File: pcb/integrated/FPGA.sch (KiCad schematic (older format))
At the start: 28 parts, among them J3001 Conn_01x04_Male, J3002 Conn_01x06_Male, U3001 XC7S25-L1FTGB196, U3002 S25FL127SABN, U3003 74AVC4TD245BQ

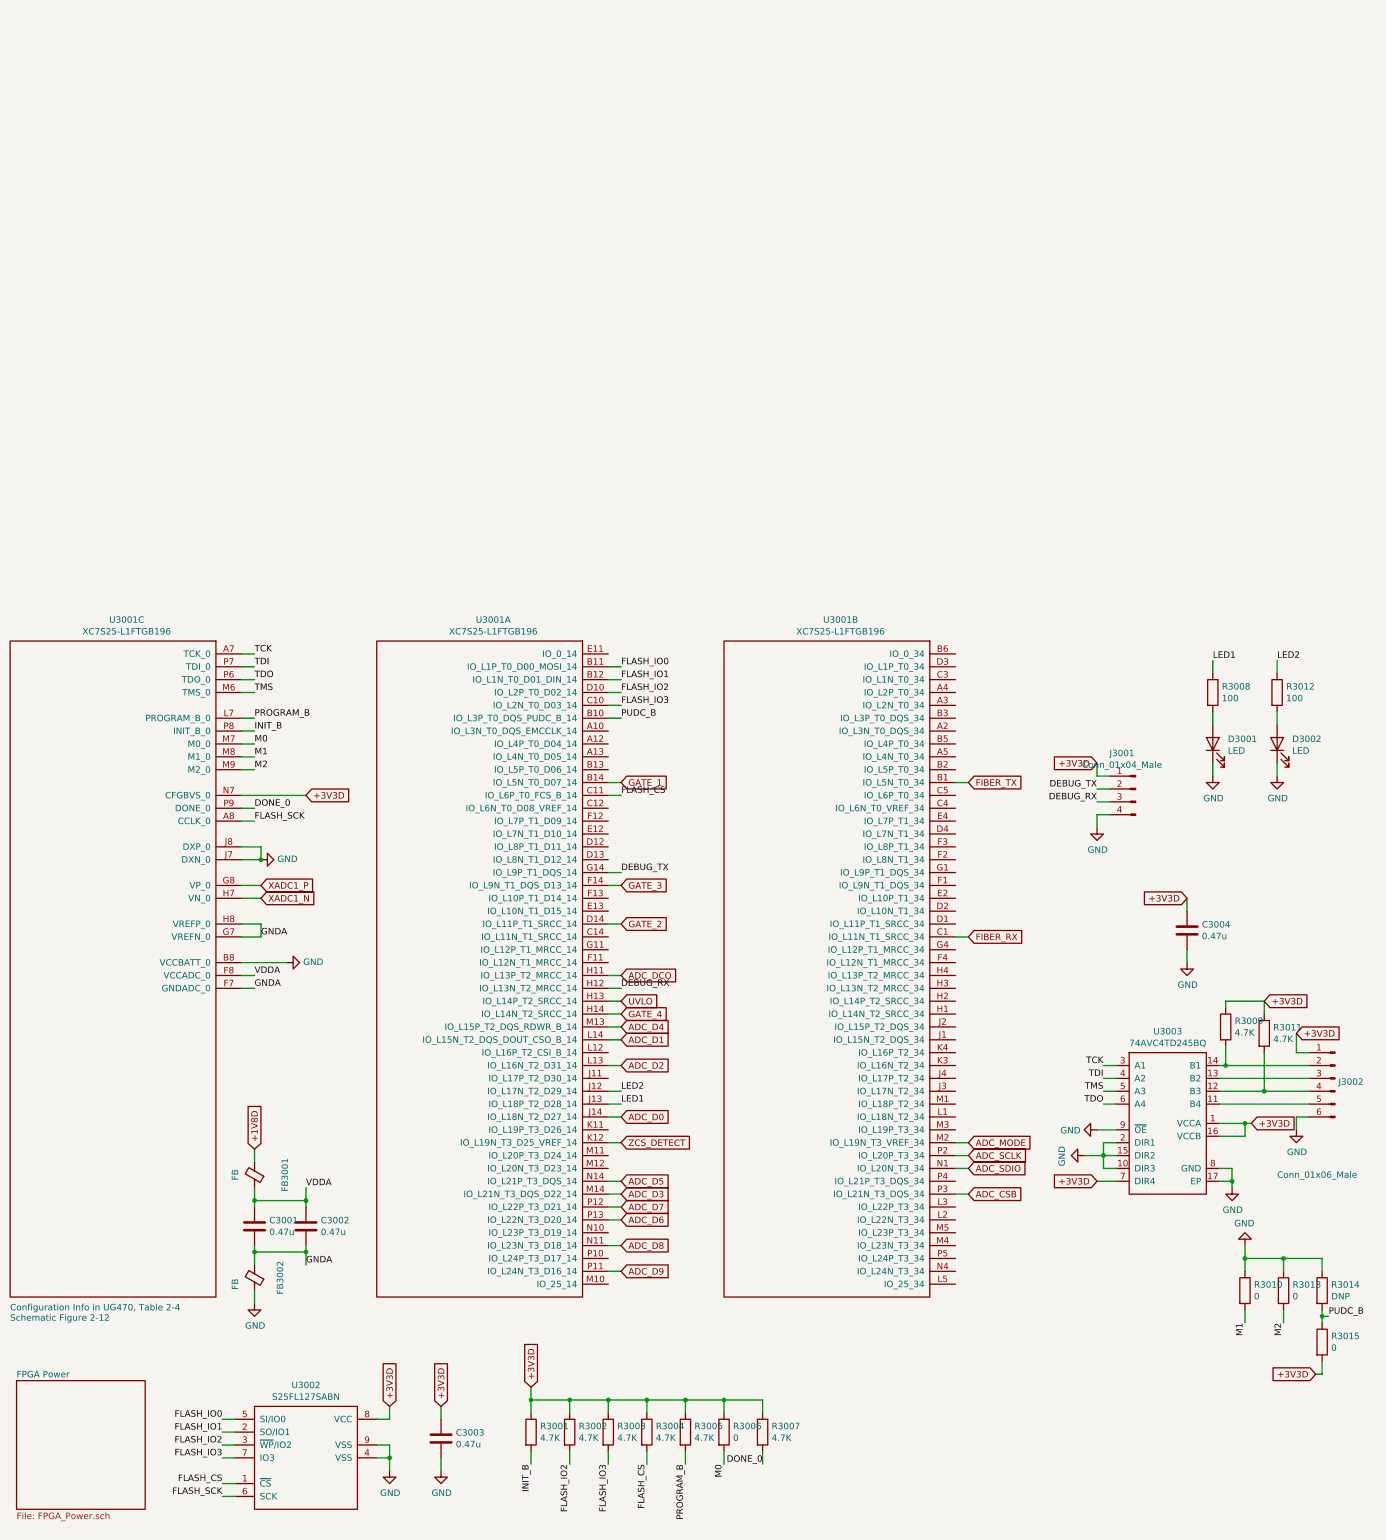
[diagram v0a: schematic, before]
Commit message: schematic fixes and component placement
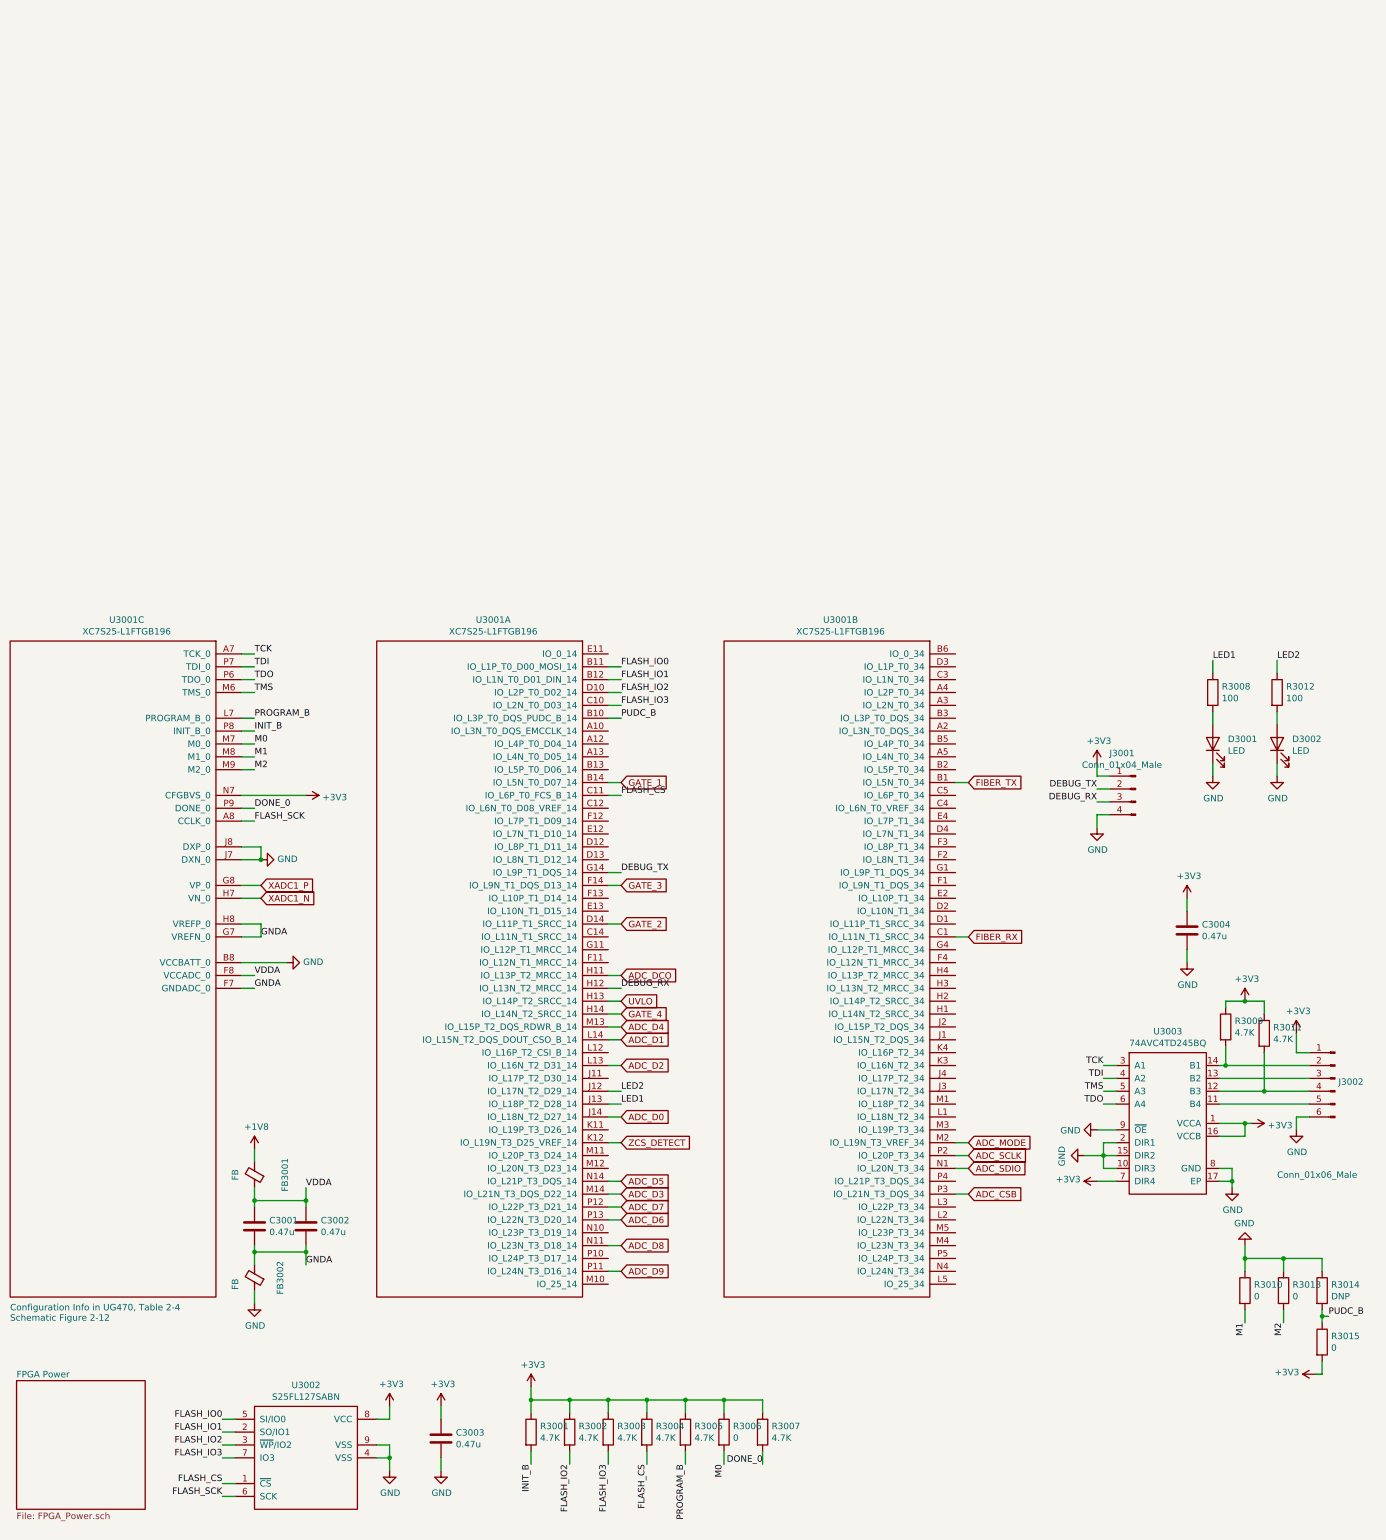
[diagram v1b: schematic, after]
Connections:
- net +1V8D renamed +1V8
- net +3V3D renamed +3V3
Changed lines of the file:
@@
 Wire Wire Line
 	2450 1950 2950 1950
-Text GLabel 3600 6700 1    50   Input ~ 0
-+3V3D
-Text GLabel 4000 6700 1    50   Input ~ 0
-+3V3D
-Text GLabel 4700 6550 1    50   Input ~ 0
-+3V3D
-Text GLabel 9100 4950 0    50   Input ~ 0
-+3V3D
-Text GLabel 10650 3800 2    50   Input ~ 0
-+3V3D
-Text GLabel 9800 2750 0    50   Input ~ 0
-+3V3D
-Text GLabel 2950 1950 2    50   Input ~ 0
-+3V3D
-Text GLabel 2550 4700 1    50   Input ~ 0
-+1V8D
 Wire Wire Line
 	5300 3350 5400 3350
@@
 Wire Wire Line
 	10850 6000 10850 6050
-Text GLabel 10800 6450 0    50   Input ~ 0
-+3V3D
 Wire Wire Line
 	10850 6350 10850 6450
@@
 	-1   0    0    -1
 $EndComp
-Text GLabel 10300 4500 2    50   Input ~ 0
-+3V3D
 Wire Wire Line
 	5300 1850 5400 1850
@@
 Wire Wire Line
 	9200 1900 9100 1900
-Text GLabel 9100 1700 0    50   Input ~ 0
-+3V3D
 Wire Wire Line
 	9100 1700 9100 1800
@@
 Wire Wire Line
 	10100 4050 10750 4050
-Text GLabel 10400 3550 2    50   Input ~ 0
-+3V3D
 Wire Wire Line
 	10100 3600 10100 3550
@@
 	10400 3650 10400 3550
 Wire Wire Line
-	10100 3550 10400 3550
+	10100 3550 10250 3550
 $Comp
 L Device:Ferrite_Bead_Small FB3002
@@
 Text GLabel 2600 2750 2    50   Input ~ 0
 XADC1_N
+$Comp
+L power:+3V3 #PWR0111
+U 1 1 5D7E33C3
+P 10250 3550
+F 0 "#PWR0111" H 10250 3400 50  0001 C CNN
+F 1 "+3V3" H 10265 3723 50  0000 C CNN
+F 2 "" H 10250 3550 50  0001 C CNN
+F 3 "" H 10250 3550 50  0001 C CNN
+	1    10250 3550
+	1    0    0    -1
+$EndComp
+Connection ~ 10250 3550
+Wire Wire Line
+	10250 3550 10400 3550
+$Comp
+L power:+3V3 #PWR0154
+U 1 1 5D7E45AF
+P 10650 3800
+F 0 "#PWR0154" H 10650 3650 50  0001 C CNN
+F 1 "+3V3" H 10665 3973 50  0000 C CNN
+F 2 "" H 10650 3800 50  0001 C CNN
+F 3 "" H 10650 3800 50  0001 C CNN
+	1    10650 3800
+	1    0    0    -1
+$EndComp
+$Comp
+L power:+3V3 #PWR0155
+U 1 1 5D7E4D28
+P 10300 4500
+F 0 "#PWR0155" H 10300 4350 50  0001 C CNN
+F 1 "+3V3" V 10315 4628 50  0000 L CNN
+F 2 "" H 10300 4500 50  0001 C CNN
+F 3 "" H 10300 4500 50  0001 C CNN
+	1    10300 4500
+	0    1    1    0
+$EndComp
+$Comp
+L power:+3V3 #PWR0156
+U 1 1 5D7E57D1
+P 9100 4950
+F 0 "#PWR0156" H 9100 4800 50  0001 C CNN
+F 1 "+3V3" V 9115 5078 50  0000 L CNN
+F 2 "" H 9100 4950 50  0001 C CNN
+F 3 "" H 9100 4950 50  0001 C CNN
+	1    9100 4950
+	0    -1   -1   0
+$EndComp
+$Comp
+L power:+3V3 #PWR0157
+U 1 1 5D7E5FC2
+P 10800 6450
+F 0 "#PWR0157" H 10800 6300 50  0001 C CNN
+F 1 "+3V3" V 10815 6578 50  0000 L CNN
+F 2 "" H 10800 6450 50  0001 C CNN
+F 3 "" H 10800 6450 50  0001 C CNN
+	1    10800 6450
+	0    -1   -1   0
+$EndComp
+$Comp
+L power:+3V3 #PWR0158
+U 1 1 5D7E66BA
+P 4700 6550
+F 0 "#PWR0158" H 4700 6400 50  0001 C CNN
+F 1 "+3V3" H 4715 6723 50  0000 C CNN
+F 2 "" H 4700 6550 50  0001 C CNN
+F 3 "" H 4700 6550 50  0001 C CNN
+	1    4700 6550
+	1    0    0    -1
+$EndComp
+$Comp
+L power:+3V3 #PWR0159
+U 1 1 5D7E72F0
+P 4000 6700
+F 0 "#PWR0159" H 4000 6550 50  0001 C CNN
+F 1 "+3V3" H 4015 6873 50  0000 C CNN
+F 2 "" H 4000 6700 50  0001 C CNN
+F 3 "" H 4000 6700 50  0001 C CNN
+	1    4000 6700
+	1    0    0    -1
+$EndComp
+$Comp
+L power:+3V3 #PWR0160
+U 1 1 5D7E77C0
+P 3600 6700
+F 0 "#PWR0160" H 3600 6550 50  0001 C CNN
+F 1 "+3V3" H 3615 6873 50  0000 C CNN
+F 2 "" H 3600 6700 50  0001 C CNN
+F 3 "" H 3600 6700 50  0001 C CNN
+	1    3600 6700
+	1    0    0    -1
+$EndComp
+$Comp
+L power:+3V3 #PWR0161
+U 1 1 5D7E7BF9
+P 9800 2750
+F 0 "#PWR0161" H 9800 2600 50  0001 C CNN
+F 1 "+3V3" H 9815 2923 50  0000 C CNN
+F 2 "" H 9800 2750 50  0001 C CNN
+F 3 "" H 9800 2750 50  0001 C CNN
+	1    9800 2750
+	1    0    0    -1
+$EndComp
+$Comp
+L power:+3V3 #PWR0162
+U 1 1 5D7E7FB3
+P 9100 1700
+F 0 "#PWR0162" H 9100 1550 50  0001 C CNN
+F 1 "+3V3" H 9115 1873 50  0000 C CNN
+F 2 "" H 9100 1700 50  0001 C CNN
+F 3 "" H 9100 1700 50  0001 C CNN
+	1    9100 1700
+	1    0    0    -1
+$EndComp
+$Comp
+L power:+1V8 #PWR0163
+U 1 1 5D7E8C3A
+P 2550 4700
+F 0 "#PWR0163" H 2550 4550 50  0001 C CNN
+F 1 "+1V8" H 2565 4873 50  0000 C CNN
+F 2 "" H 2550 4700 50  0001 C CNN
+F 3 "" H 2550 4700 50  0001 C CNN
+	1    2550 4700
+	1    0    0    -1
+$EndComp
+$Comp
+L power:+3V3 #PWR0164
+U 1 1 5D7E9482
+P 2950 1950
+F 0 "#PWR0164" H 2950 1800 50  0001 C CNN
+F 1 "+3V3" V 2965 2078 50  0000 L CNN
+F 2 "" H 2950 1950 50  0001 C CNN
+F 3 "" H 2950 1950 50  0001 C CNN
+	1    2950 1950
+	0    1    1    0
+$EndComp
 $EndSCHEMATC
